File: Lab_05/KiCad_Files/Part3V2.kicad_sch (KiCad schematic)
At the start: 0 parts

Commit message: Continue Lab 5
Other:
- company: (none) -> Jim Horwitz & Mark Vaughn, Jork Incorporated
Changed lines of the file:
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@@
 (kicad_sch (version 20230121) (generator eeschema)
   (paper "A4")
+  (title_block
+    (date "2024-02-17")
+    (company "Jim Horwitz & Mark Vaughn, Jork Incorporated")
+  )
 )

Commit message: Finish Saturday Schematics
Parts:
- added C103: 2.2uF, symbol Device:C_Polarized_US
- added C103: 1uF, symbol Device:C_Polarized_US
- added C104 (x2): 47uF, symbol Device:C_Polarized_US
- added C401: 1uF, symbol Device:C
- added L101 (x2): 4mH, symbol Device:L
- added LA301: ${SIM.PARAMS}, symbol Device:Lamp
- added Q110 (x5): NPN, symbol Simulation_SPICE:NPN
- added Q2: PNP, symbol Simulation_SPICE:PNP
- added R115 (x2): 47K, symbol Device:R
- added R116 (x7), R118: 10K, symbol Device:R
- added R117 (x3), R119: 1K, symbol Device:R
- added R117 (x2): 680R, symbol Device:R
- added R118 (x2): 2K7, symbol Device:R
- added R119 (x2): 100R, symbol Device:R
- added V1: VSIN_P3B, symbol Simulation_SPICE:VSIN
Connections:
- new net: Q110.1 (C), Q2.2 (B), R116.1, R117.2
- new net: Q110.2 (B), R116.2, R116.2 (x2)
- new net: Q110.1 (C), R115.1, R115.1, R118.2
- new net: C103.1, C104.2, L101.1, R115.2 (x2)
- new net: Q110.3 (E), R119.1 (x3)
- new net: C104.1, Q110.2 (B), R116.2, R117.1 (x2)
- new net: LA301.2 (+), Q2.1 (C)
- new net: C401.2, Q110.2 (B), R116.2, R117.1
- new net: Q110.1 (C), R116.1, R117.2
- new net: C401.1, V1.1
- new net +15V: Q2.3 (E), R116.1, R116.1, R116.1, R117.1, R117.1, R118.1, R118.1, R118.1
- new net GND: C103.2, C103.2, L101.2, L101.2, LA301.1 (-), Q110.3 (E), Q110.3 (E), R117.2, R117.2, R117.2, R119.2, R119.2, R119.2, V1.2
- new net RESET: Q110.1 (C), R116.1, R118.2
- new net SET: Q110.1 (C), R116.1, R118.2
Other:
- note added: ".ac dec 100 1 10Meg"
- note added: "As the frequency of V_in (f_in) is swept, each resonant circuit will reduce V_in until f_in = f_res_hi or f_res_lo. At either point, the output of the respective tank circuit will be amplified enough to either set or reset the latch, thus turning the lamp on/off"
- note added: "Gain Stage"
- note added: "High-Frequency Tank"
- note added: "Low-Frequency Tank"
- note added: "SR Latch"
- note added: "f_res_hi = 2.51kHz"
- note added: "f_res_lo = 1.69kHz"
- title: (none) -> Frequency Detecting Lamp

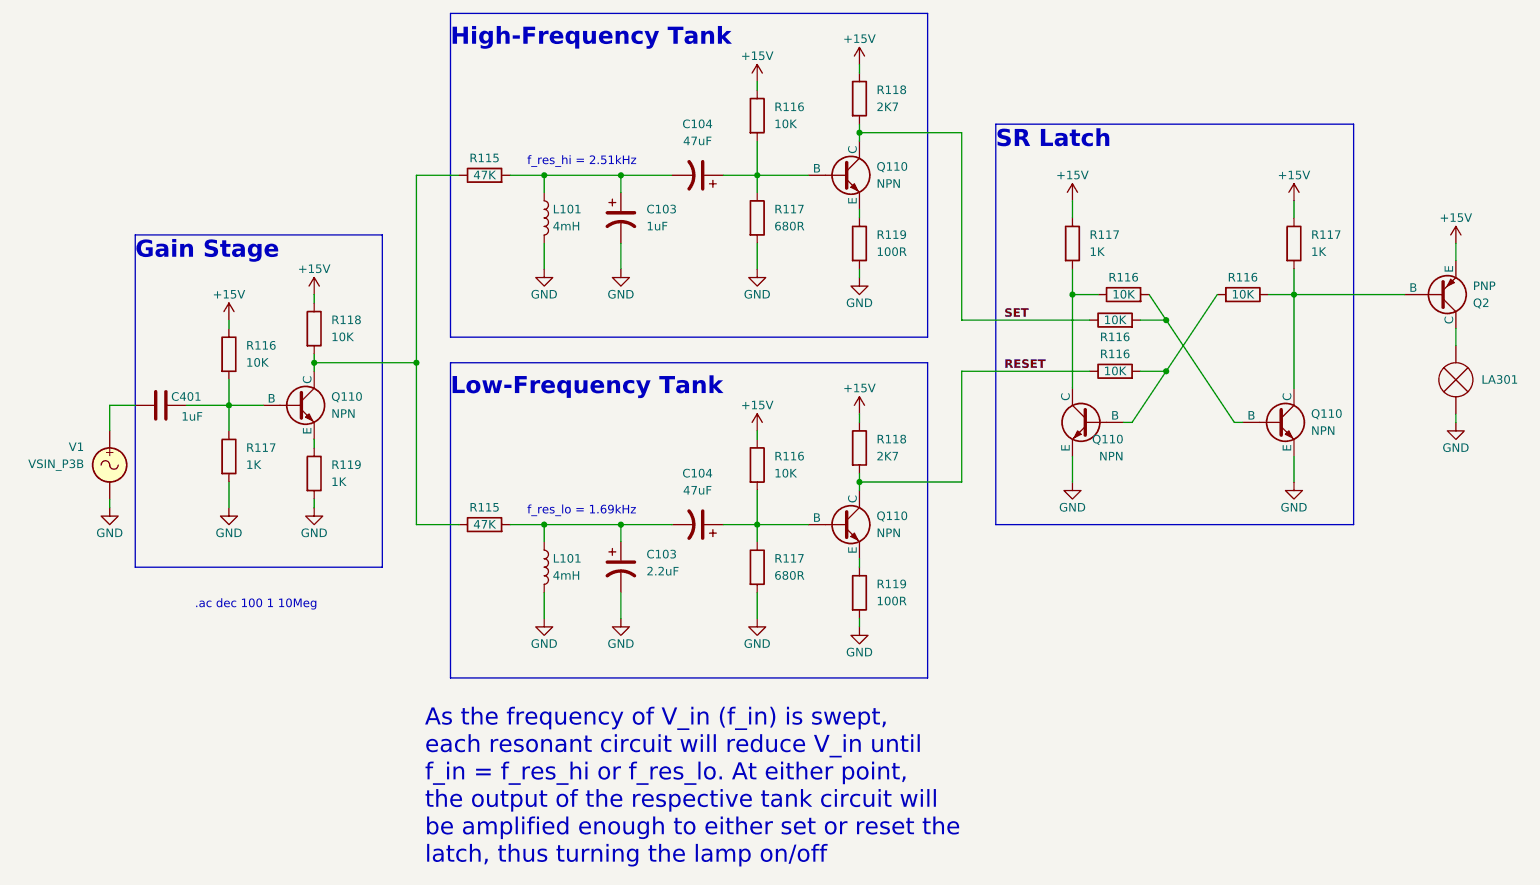
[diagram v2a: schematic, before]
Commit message: Revise part 3 Version 1
For next revision:
- add collector resistor to Q304
- remove R309
- add emitter follower after integrator
For the future:
- add more poles to bandpass!!
- maybe a resonant filter?
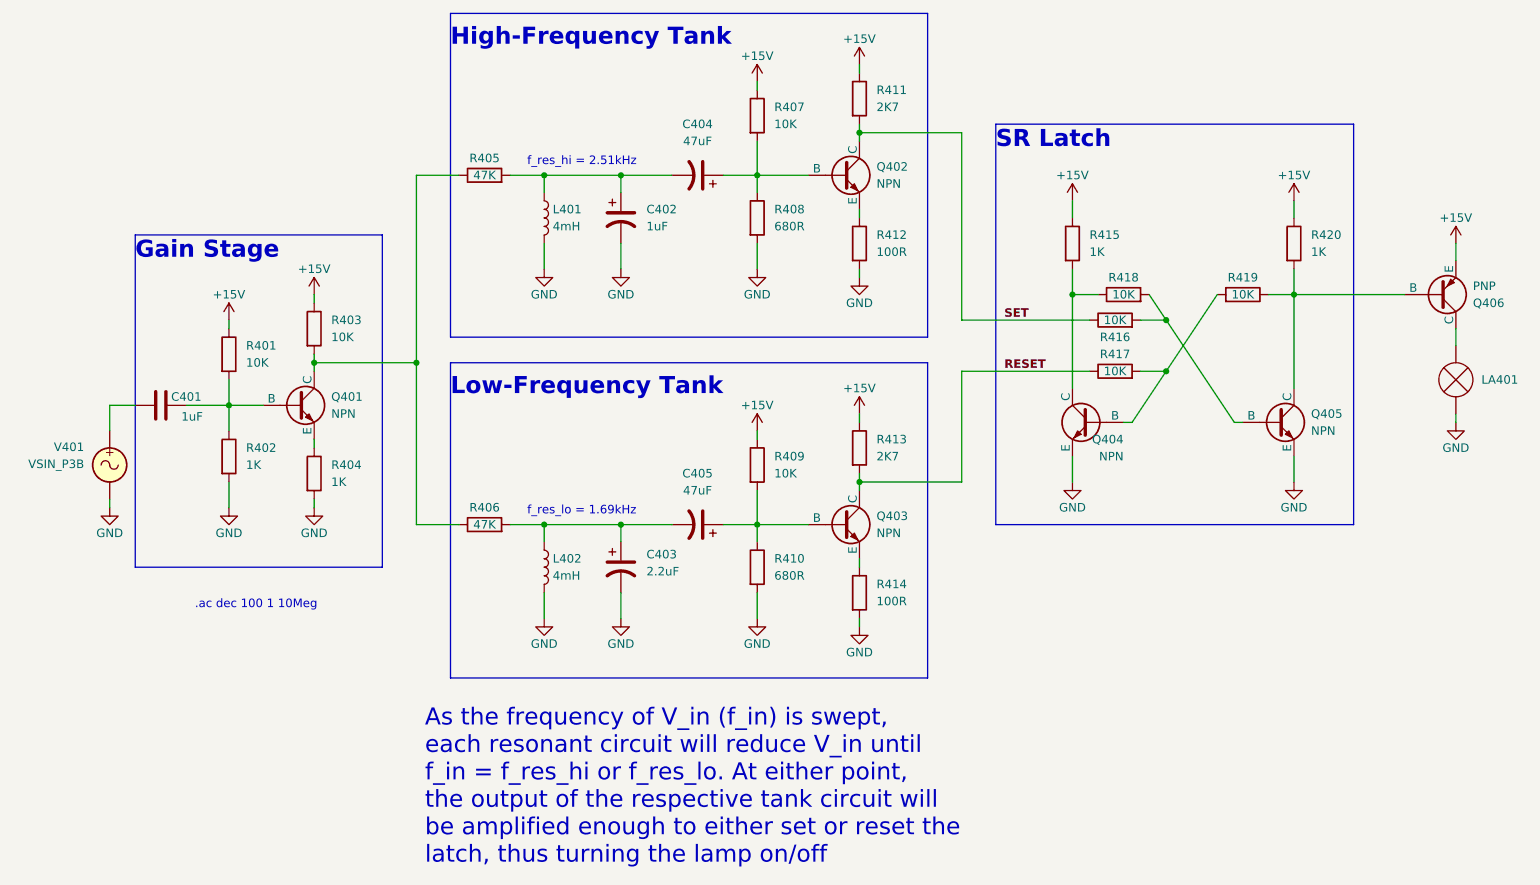
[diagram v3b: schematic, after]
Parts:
- renumbered C103 to C402, C103 to C403, C104 to C404, C104 to C405, L101 to L401, L101 to L402, LA301 to LA401, Q110 to Q401, Q110 to Q402, Q110 to Q403, Q110 to Q404, Q110 to Q405, Q2 to Q406, R116 to R401, R117 to R402, R118 to R403, R119 to R404, R115 to R405, R115 to R406, R116 to R407, R117 to R408, R116 to R409, R117 to R410, R118 to R411, R119 to R412, R118 to R413, R119 to R414, R117 to R415, R116 to R416, R116 to R417, R116 to R418, R116 to R419, R117 to R420, V1 to V401

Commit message: Finish Lab 5
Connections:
- net +15V renamed VCC
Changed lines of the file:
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@@
     )
   )
-  (symbol (lib_id "power:+15V") (at 247.65 69.85 0) (unit 1)
+  (symbol (lib_id "power:VCC") (at 247.65 69.85 0) (unit 1)
     (in_bom yes) (on_board yes) (dnp no)
     (property "Reference" "#PWR0422" (at 247.65 73.66 0)
       (effects (font (size 1.27 1.27)) hide)
     )
-    (property "Value" "+15V" (at 247.65 66.04 0)
+    (property "Value" "VCC" (at 247.65 66.04 0)
       (effects (font (size 1.27 1.27)))
     )
@@
     )
   )
-  (symbol (lib_id "power:+15V") (at 64.77 81.28 0) (unit 1)
+  (symbol (lib_id "power:VCC") (at 64.77 81.28 0) (unit 1)
     (in_bom yes) (on_board yes) (dnp no)
     (property "Reference" "#PWR0402" (at 64.77 85.09 0)
       (effects (font (size 1.27 1.27)) hide)
     )
-    (property "Value" "+15V" (at 64.77 77.47 0)
+    (property "Value" "VCC" (at 64.77 77.47 0)
       (effects (font (size 1.27 1.27)))
     )
@@
     )
   )
-  (symbol (lib_id "power:+15V") (at 143.51 97.79 0) (unit 1)
+  (symbol (lib_id "power:VCC") (at 143.51 97.79 0) (unit 1)
     (in_bom yes) (on_board yes) (dnp no)
     (property "Reference" "#PWR0412" (at 143.51 101.6 0)
       (effects (font (size 1.27 1.27)) hide)
     )
-    (property "Value" "+15V" (at 143.51 93.98 0)
+    (property "Value" "VCC" (at 143.51 93.98 0)
       (effects (font (size 1.27 1.27)))
     )
@@
     )
   )
-  (symbol (lib_id "power:+15V") (at 143.51 45.72 0) (unit 1)
+  (symbol (lib_id "power:VCC") (at 143.51 45.72 0) (unit 1)
     (in_bom yes) (on_board yes) (dnp no)
     (property "Reference" "#PWR0410" (at 143.51 49.53 0)
       (effects (font (size 1.27 1.27)) hide)
     )
-    (property "Value" "+15V" (at 143.51 41.91 0)
+    (property "Value" "VCC" (at 143.51 41.91 0)
       (effects (font (size 1.27 1.27)))
     )
@@
     )
   )
-  (symbol (lib_id "power:+15V") (at 190.5 63.5 0) (unit 1)
+  (symbol (lib_id "power:VCC") (at 190.5 63.5 0) (unit 1)
     (in_bom yes) (on_board yes) (dnp no)
     (property "Reference" "#PWR0418" (at 190.5 67.31 0)
       (effects (font (size 1.27 1.27)) hide)
     )
-    (property "Value" "+15V" (at 190.5 59.69 0)
+    (property "Value" "VCC" (at 190.5 59.69 0)
       (effects (font (size 1.27 1.27)))
     )
@@
     )
   )
-  (symbol (lib_id "power:+15V") (at 223.52 63.5 0) (unit 1)
+  (symbol (lib_id "power:VCC") (at 223.52 63.5 0) (unit 1)
     (in_bom yes) (on_board yes) (dnp no)
     (property "Reference" "#PWR0420" (at 223.52 67.31 0)
       (effects (font (size 1.27 1.27)) hide)
     )
-    (property "Value" "+15V" (at 223.52 59.69 0)
+    (property "Value" "VCC" (at 223.52 59.69 0)
       (effects (font (size 1.27 1.27)))
     )
@@
     )
   )
-  (symbol (lib_id "power:+15V") (at 158.75 43.18 0) (unit 1)
+  (symbol (lib_id "power:VCC") (at 158.75 43.18 0) (unit 1)
     (in_bom yes) (on_board yes) (dnp no)
     (property "Reference" "#PWR0414" (at 158.75 46.99 0)
       (effects (font (size 1.27 1.27)) hide)
     )
-    (property "Value" "+15V" (at 158.75 39.37 0)
+    (property "Value" "VCC" (at 158.75 39.37 0)
       (effects (font (size 1.27 1.27)))
     )
@@
     )
   )
-  (symbol (lib_id "power:+15V") (at 77.47 77.47 0) (unit 1)
+  (symbol (lib_id "power:VCC") (at 77.47 77.47 0) (unit 1)
     (in_bom yes) (on_board yes) (dnp no)
     (property "Reference" "#PWR0404" (at 77.47 81.28 0)
       (effects (font (size 1.27 1.27)) hide)
     )
-    (property "Value" "+15V" (at 77.47 73.66 0)
+    (property "Value" "VCC" (at 77.47 73.66 0)
       (effects (font (size 1.27 1.27)))
     )
@@
     )
   )
-  (symbol (lib_id "power:+15V") (at 158.75 95.25 0) (unit 1)
+  (symbol (lib_id "power:VCC") (at 158.75 95.25 0) (unit 1)
     (in_bom yes) (on_board yes) (dnp no)
     (property "Reference" "#PWR0416" (at 158.75 99.06 0)
       (effects (font (size 1.27 1.27)) hide)
     )
-    (property "Value" "+15V" (at 158.75 91.44 0)
-      (effects (font (size 1.27 1.27)))
-    )
+    (property "Value" "VCC" (at 158.75 91.44 0)
+      (effects (font (size 1.27 1.27)))
+    )
